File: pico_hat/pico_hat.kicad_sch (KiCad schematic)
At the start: 20 parts, among them J1 Conn_01x07_Male, J2 Conn_01x02_Female, J3 Barrel_Jack, J4 WROOM32_1, J5 WROOM32_2, Q1 NDT3055, U1 L7805

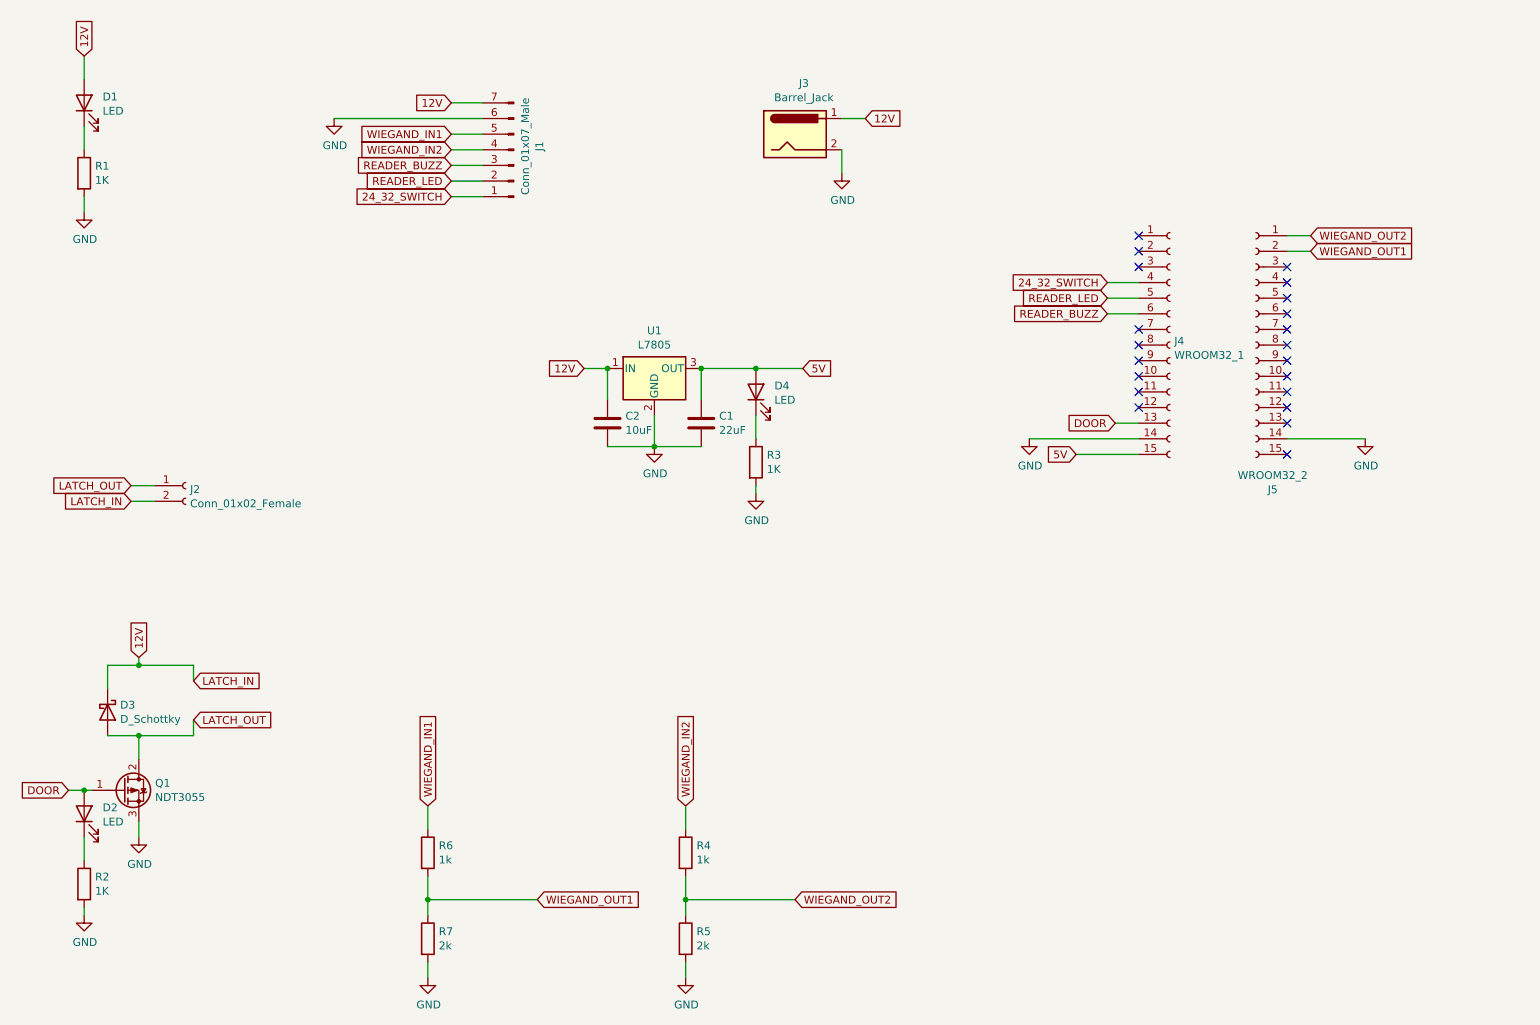
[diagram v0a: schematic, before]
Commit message: Add screen pin. Remove two of the three LEDs. Sense input.
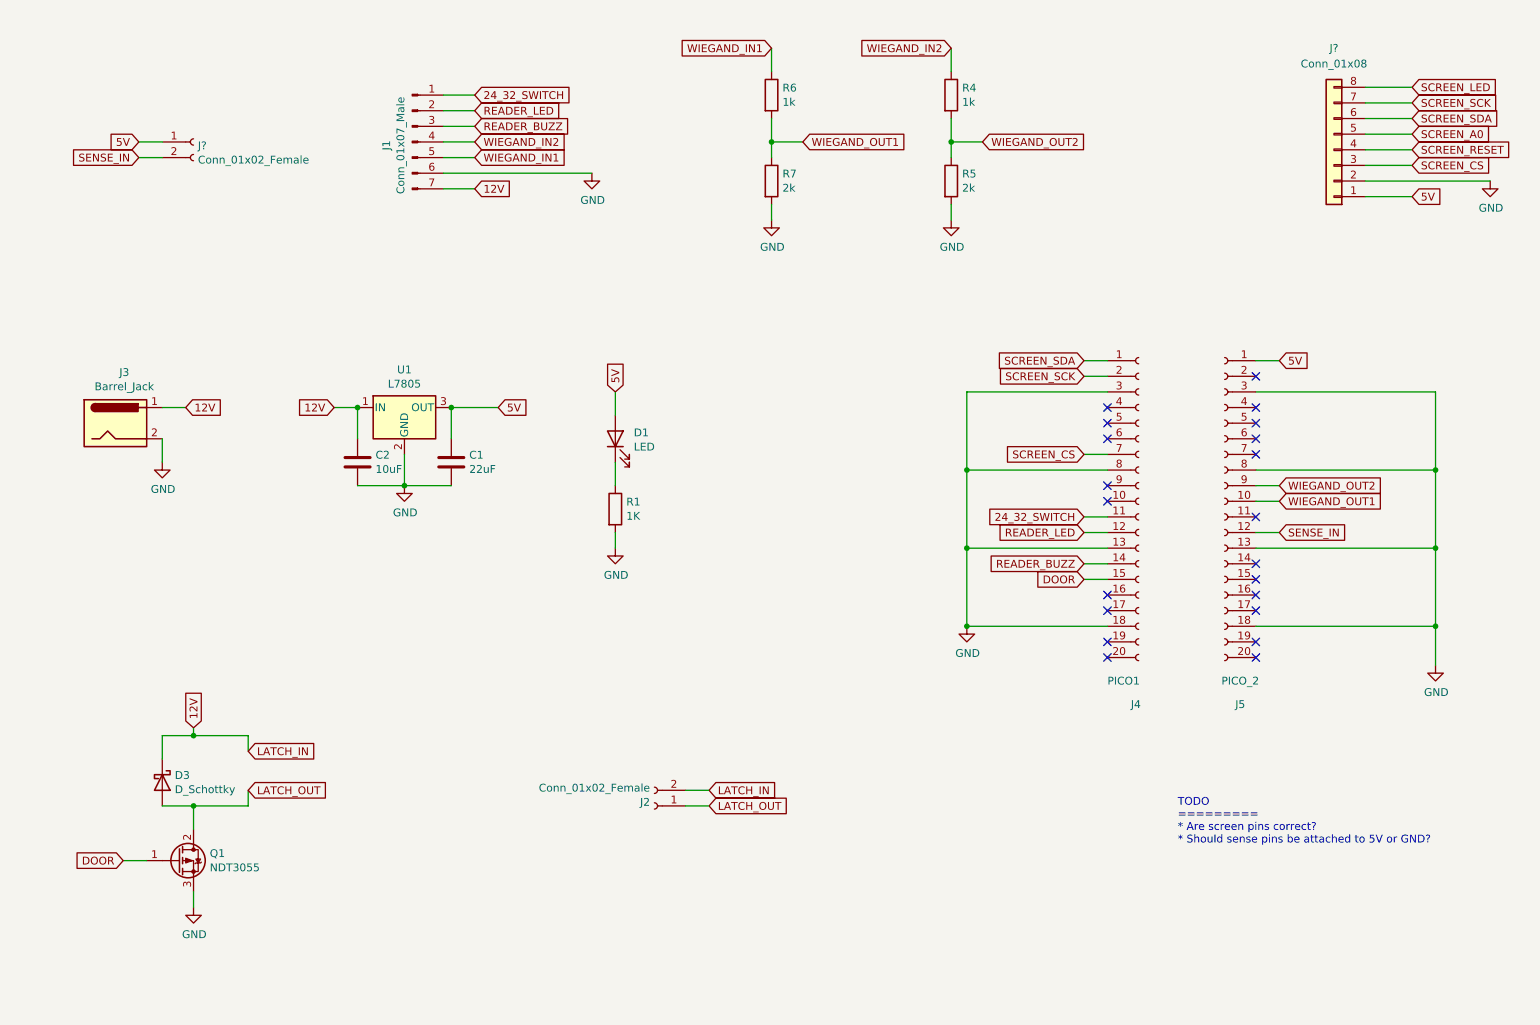
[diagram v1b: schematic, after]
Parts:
- removed D2, D4: LED, LEDs:LED-1206, symbol Device:LED
- removed R2, R3: 1K, Resistors_SMD:R_1210, symbol Device:R
- added J?: Conn_01x02_Female, Terminal_Blocks:TerminalBlock_Pheonix_MKDS1.5-2pol, symbol Connector:Conn_01x02_Female
- added J?: Conn_01x08, symbol Connector_Generic:Conn_01x08
- J1: Digikey # (none) -> 455-B7B-XH-A-ND
- J4: value WROOM32_1 -> PICO1; symbol Connector:Conn_01x15_Female -> Connector:Conn_01x20_Female
- J5: value WROOM32_2 -> PICO_2; symbol Connector:Conn_01x15_Female -> Connector:Conn_01x20_Female
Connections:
- net 12V: no longer D1.2 (A)
- net 24_32_SWITCH: now also J4.11 (Pin_11); no longer J4.4 (Pin_4)
- net 5V: now also D1.2 (A), J5.1 (Pin_1), J?.1 (Pin_1), J?.1 (Pin_1); no longer J4.15 (Pin_15)
- net DOOR: now also J4.15 (Pin_15); no longer J4.13 (Pin_13)
- net GND: now also J4.13 (Pin_13), J4.18 (Pin_18), J4.3 (Pin_3), J4.8 (Pin_8), J5.13 (Pin_13), J5.18 (Pin_18), J5.3 (Pin_3), J5.8 (Pin_8), J?.2 (Pin_2); no longer J4.14 (Pin_14), J5.14 (Pin_14)
- net READER_BUZZ: now also J4.14 (Pin_14); no longer J4.6 (Pin_6)
- net READER_LED: now also J4.12 (Pin_12); no longer J4.5 (Pin_5)
- net WIEGAND_OUT1: now also J5.10 (Pin_10); no longer J5.2 (Pin_2)
- net WIEGAND_OUT2: now also J5.9 (Pin_9); no longer J5.1 (Pin_1)
- net SCREEN_SDA: now reaches J4.1 (Pin_1)
- net SCREEN_SDA: now also J?.6 (Pin_6)
- net SCREEN_SCK: now reaches J4.2 (Pin_2)
- net SCREEN_SCK: now also J?.7 (Pin_7)
- net SCREEN_CS: now reaches J4.7 (Pin_7)
- net SCREEN_CS: now also J?.3 (Pin_3)
- net SENSE_IN: now reaches J5.12 (Pin_12)
- net SENSE_IN: now also J?.2 (Pin_2)
- new net SCREEN_A0: J?.5 (Pin_5)
- new net SCREEN_LED: J?.8 (Pin_8)
- new net SCREEN_RESET: J?.4 (Pin_4)
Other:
- note added: "TODO ========= * Are screen pins correct? * Should sense pins be attached to 5V or GND?"
- moved on the sheet: C1, C2, D1, D3, J1, J2, J3, Q1, R1, R4, R5, R6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

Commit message: Remove extra LEDs. Connectors for screen and sense input. Move to Pi Pico.
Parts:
- removed J?: Conn_01x02_Female, Terminal_Blocks:TerminalBlock_Pheonix_MKDS1.5-2pol, symbol Connector:Conn_01x02_Female
- removed J?: Conn_01x08, symbol Connector_Generic:Conn_01x08
- added J?: Conn_01x03, symbol Connector_Generic:Conn_01x03
- added J?: Conn_01x11, symbol Connector_Generic:Conn_01x11
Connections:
- net 5V: now also J5.2 (Pin_2), J?.1 (Pin_1), J?.1 (Pin_1); no longer J5.1 (Pin_1)
- net GND: now also J?.2 (Pin_2), J?.2 (Pin_2)
- net SCREEN_A0: now also J?.5 (Pin_5)
- net SCREEN_CS: now also J?.3 (Pin_3)
- net SCREEN_LED: now also J?.8 (Pin_8)
- net SCREEN_RESET: now also J?.4 (Pin_4)
- net SCREEN_SCK: now also J?.7 (Pin_7)
- net SCREEN_SDA: now also J?.6 (Pin_6)
- net SENSE_IN: now also J?.3 (Pin_3)
- net SCREEN_BTN1: now reaches J5.17 (Pin_17)
- net SCREEN_BTN1: now also J?.11 (Pin_11)
- net SCREEN_BTN2: now reaches J5.19 (Pin_19)
- net SCREEN_BTN2: now also J?.10 (Pin_10)
- net SCREEN_BTN3: now reaches J5.20 (Pin_20)
- net SCREEN_BTN3: now also J?.9 (Pin_9)
- net DOOR renamed LATCH
- no-connect marks 21 -> 18
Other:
- note added: "TODO ========= * Are screen pins correct?"
- note removed: "TODO ========= * Are screen pins correct? * Should sense pins be attached to 5V or GND?"
- moved on the sheet: C1, C2, D1, R1, U1
